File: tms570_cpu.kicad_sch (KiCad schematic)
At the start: 54 parts, among them J12 TSW-103-08-F-S-RA, J3 FTSH-105-01-L-DV-K, U2 TMS570LS0914APGEQQ1

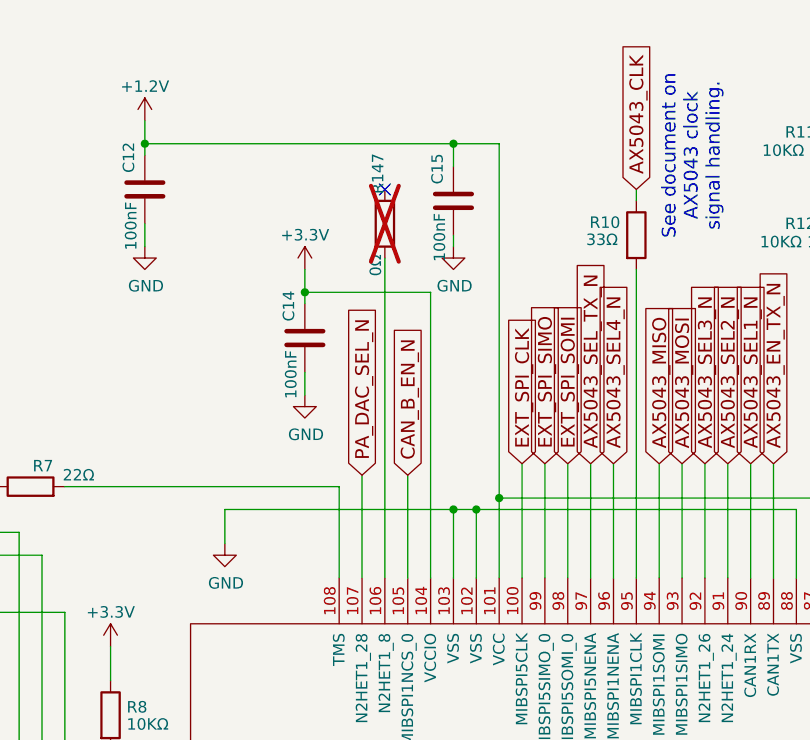
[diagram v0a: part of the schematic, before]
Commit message: Add switches on SPI to PC104, rework ICD and Design docs
Signed-off-by: Corey Minyard <corey@minyard.net>
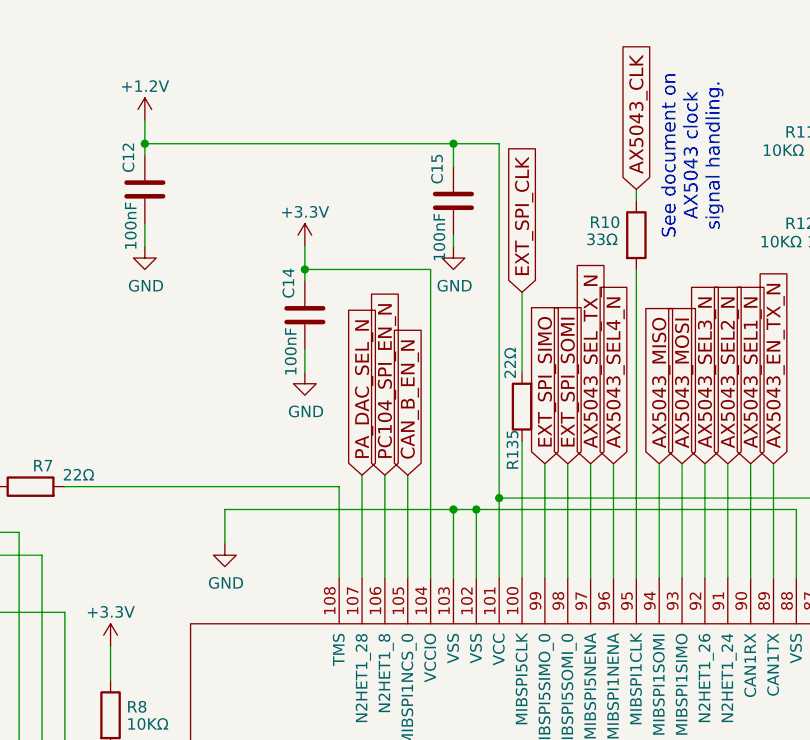
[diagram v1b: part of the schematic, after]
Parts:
- removed R147: 0Ω, Resistor_SMD:R_0402_1005Metric_Pad0.72x0.64mm_HandSolder, symbol Device:R
- added R135: 22Ω, Resistor_SMD:R_0402_1005Metric_Pad0.72x0.64mm_HandSolder, symbol Device:R
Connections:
- net EXT_SPI_CLK: now also R135.2; no longer U2.100 (MIBSPI5CLK)
- net PC104_SPI_EN_N: now reaches U2.106 (N2HET1_8)
- new net: R135.1, U2.100 (MIBSPI5CLK)
- no-connect marks 6 -> 5
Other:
- moved on the sheet: C14
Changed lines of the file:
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@@
 	)
 	(junction
-		(at 167.64 40.64)
+		(at 167.64 38.1)
 		(diameter 0)
 		(color 0 0 0 0)
@@
 	)
 	(no_connect
-		(at 176.53 29.21)
-	)
-	(no_connect
 		(at 247.65 52.07)
 	)
@@
 	(wire
 		(pts
-			(xy 167.64 49.53) (xy 167.64 52.07)
+			(xy 167.64 46.99) (xy 167.64 49.53)
 		)
 		(stroke
@@
 	(wire
 		(pts
-			(xy 167.64 38.1) (xy 167.64 40.64)
+			(xy 167.64 35.56) (xy 167.64 38.1)
 		)
 		(stroke
@@
 	(wire
 		(pts
+			(xy 176.53 60.96) (xy 176.53 72.39)
+		)
+		(stroke
+			(width 0)
+			(type default)
+		)
+	)
+	(wire
+		(pts
 			(xy 207.01 204.47) (xy 207.01 226.06)
 		)
@@
 	(wire
 		(pts
-			(xy 167.64 40.64) (xy 167.64 41.91)
+			(xy 167.64 38.1) (xy 167.64 39.37)
 		)
 		(stroke
@@
 	(wire
 		(pts
-			(xy 176.53 36.83) (xy 176.53 72.39)
-		)
-		(stroke
-			(width 0)
-			(type default)
-		)
-	)
-	(wire
-		(pts
 			(xy 110.49 187.96) (xy 116.84 187.96)
 		)
@@
 	(wire
 		(pts
-			(xy 181.61 40.64) (xy 181.61 72.39)
+			(xy 181.61 38.1) (xy 181.61 72.39)
 		)
 		(stroke
@@
 	(wire
 		(pts
-			(xy 167.64 40.64) (xy 181.61 40.64)
+			(xy 167.64 38.1) (xy 181.61 38.1)
 		)
 		(stroke
@@
 	(wire
 		(pts
+			(xy 191.77 57.15) (xy 191.77 72.39)
+		)
+		(stroke
+			(width 0)
+			(type default)
+		)
+	)
+	(wire
+		(pts
 			(xy 281.94 137.16) (xy 293.37 137.16)
 		)
@@
 	(wire
 		(pts
-			(xy 191.77 59.69) (xy 191.77 72.39)
+			(xy 191.77 40.64) (xy 191.77 49.53)
 		)
 		(stroke
@@
 		)
 	)
+	(global_label "PC104_SPI_EN_N"
+		(shape input)
+		(at 176.53 60.96 90)
+		(fields_autoplaced yes)
+		(effects
+			(font
+				(size 1.524 1.524)
+			)
+			(justify left)
+		)
+		(property "Intersheetrefs" "${INTERSHEET_REFS}"
+			(at 176.53 39.0045 90)
+			(effects
+				(font
+					(size 1.27 1.27)
+				)
+				(justify left)
+				(hide yes)
+			)
+		)
+	)
 	(global_label "AX5043_EN_RX3_N"
 		(shape input)
@@
 	(global_label "EXT_SPI_CLK"
 		(shape input)
-		(at 191.77 59.69 90)
+		(at 191.77 40.64 90)
 		(fields_autoplaced yes)
 		(effects
@@
 		)
 		(property "Intersheetrefs" "${INTERSHEET_REFS}"
-			(at 191.77 42.5968 90)
+			(at 191.77 23.5468 90)
 			(effects
 				(font
@@
 	(symbol
 		(lib_id "power:GND")
-		(at 167.64 52.07 0)
+		(at 167.64 49.53 0)
 		(unit 1)
 		(exclude_from_sim no)
@@
 		(dnp no)
 		(property "Reference" "#PWR023"
-			(at 167.64 58.42 0)
+			(at 167.64 55.88 0)
 			(effects
 				(font
@@
 		)
 		(property "Value" "GND"
-			(at 167.767 56.4642 0)
+			(at 167.767 53.9242 0)
 			(effects
 				(font
@@
 		)
 		(property "Footprint" ""
-			(at 167.64 52.07 0)
+			(at 167.64 49.53 0)
 			(effects
 				(font
@@
 		)
 		(property "Datasheet" ""
-			(at 167.64 52.07 0)
+			(at 167.64 49.53 0)
 			(effects
 				(font
@@
 		)
 		(property "Description" ""
-			(at 167.64 52.07 0)
+			(at 167.64 49.53 0)
 			(effects
 				(font
@@
 	(symbol
 		(lib_id "Device:R")
-		(at 176.53 33.02 0)
-		(unit 1)
-		(exclude_from_sim no)
-		(in_bom no)
-		(on_board yes)
-		(dnp yes)
-		(property "Reference" "R147"
-			(at 175.768 29.718 90)
-			(effects
-				(font
-					(size 1.27 1.27)
-				)
-				(justify left)
-			)
-		)
-		(property "Value" "0Ω"
-			(at 175.514 38.862 90)
-			(effects
-				(font
-					(size 1.27 1.27)
-				)
-				(justify left)
-			)
-		)
-		(property "Footprint" "Resistor_SMD:R_0402_1005Metric_Pad0.72x0.64mm_HandSolder"
-			(at 174.752 33.02 90)
-			(effects
-				(font
-					(size 1.27 1.27)
-				)
-				(hide yes)
-			)
-		)
-		(property "Datasheet" "~"
-			(at 176.53 33.02 0)
-			(effects
-				(font
-					(size 1.27 1.27)
-				)
-				(hide yes)
-			)
-		)
-		(property "Description" ""
-			(at 176.53 33.02 0)
-			(effects
-				(font
-					(size 1.27 1.27)
-				)
-			)
-		)
-		(pin "1"
-		)
-		(pin "2"
-		)
-		(instances
-			(project "PacSat_AFSK"
-				(path "/cc9f42d2-6985-41ac-acab-5ab7b01c5b38/adf61ae3-df77-4e04-8bda-b4049a36fcf4"
-					(reference "R147")
-					(unit 1)
-				)
-			)
-		)
-	)
-	(symbol
-		(lib_id "Device:R")
 		(at 125.73 64.77 90)
 		(unit 1)
@@
 	(symbol
 		(lib_id "Device:C")
-		(at 167.64 45.72 0)
+		(at 167.64 43.18 0)
 		(unit 1)
 		(exclude_from_sim no)
@@
 		(dnp no)
 		(property "Reference" "C14"
-			(at 165.862 42.164 90)
+			(at 165.862 39.624 90)
 			(effects
 				(font
@@
 		)
 		(property "Value" "100nF"
-			(at 166.116 49.784 90)
+			(at 166.116 47.244 90)
 			(effects
 				(font
@@
 		)
 		(property "Footprint" "Capacitor_SMD:C_0402_1005Metric_Pad0.74x0.62mm_HandSolder"
-			(at 168.6052 49.53 0)
+			(at 168.6052 46.99 0)
 			(effects
 				(font
@@
 		)
 		(property "Datasheet" "~"
-			(at 167.64 45.72 0)
+			(at 167.64 43.18 0)
 			(effects
 				(font
@@
 		)
 		(property "Description" ""
-			(at 167.64 45.72 0)
+			(at 167.64 43.18 0)
 			(effects
 				(font
@@
 	(symbol
 		(lib_id "power:+3.3V")
-		(at 167.64 38.1 0)
+		(at 167.64 35.56 0)
 		(unit 1)
 		(exclude_from_sim no)
@@
 		(fields_autoplaced yes)
 		(property "Reference" "#PWR022"
-			(at 167.64 41.91 0)
+			(at 167.64 39.37 0)
 			(effects
 				(font
@@
 		)
 		(property "Value" "+3.3V"
-			(at 167.64 34.29 0)
+			(at 167.64 31.75 0)
 			(effects
 				(font
@@
 		)
 		(property "Footprint" ""
-			(at 167.64 38.1 0)
+			(at 167.64 35.56 0)
 			(effects
 				(font
@@
 		)
 		(property "Datasheet" ""
-			(at 167.64 38.1 0)
+			(at 167.64 35.56 0)
 			(effects
 				(font
@@
 		)
 		(property "Description" ""
-			(at 167.64 38.1 0)
+			(at 167.64 35.56 0)
 			(effects
 				(font
@@
 					(unit 1)
 				)
+			)
+		)
+	)
+	(symbol
+		(lib_id "Device:R")
+		(at 191.77 53.34 180)
+		(unit 1)
+		(exclude_from_sim no)
+		(in_bom yes)
+		(on_board yes)
+		(dnp no)
+		(property "Reference" "R135"
+			(at 190.754 55.88 90)
+			(effects
+				(font
+					(size 1.27 1.27)
+				)
+				(justify left)
+			)
+		)
+		(property "Value" "22Ω"
+			(at 190.5 46.736 90)
+			(effects
+				(font
+					(size 1.27 1.27)
+				)
+				(justify left)
+			)
+		)
+		(property "Footprint" "Resistor_SMD:R_0402_1005Metric_Pad0.72x0.64mm_HandSolder"
+			(at 193.548 53.34 90)
+			(effects
+				(font
+					(size 1.27 1.27)
+				)
+				(hide yes)
+			)
+		)
+		(property "Datasheet" "~"
+			(at 191.77 53.34 0)
+			(effects
+				(font
+					(size 1.27 1.27)
+				)
+			)
+		)
+		(property "Description" ""
+			(at 191.77 53.34 0)
+			(effects
+				(font
+					(size 1.27 1.27)
+				)
+			)
+		)
+		(pin "1"
+		)
+		(pin "2"
+		)
+		(instances
+			(project "PacSat_AFSK"
+				(path "/cc9f42d2-6985-41ac-acab-5ab7b01c5b38/adf61ae3-df77-4e04-8bda-b4049a36fcf4"
+					(reference "R135")
+					(unit 1)
+				)

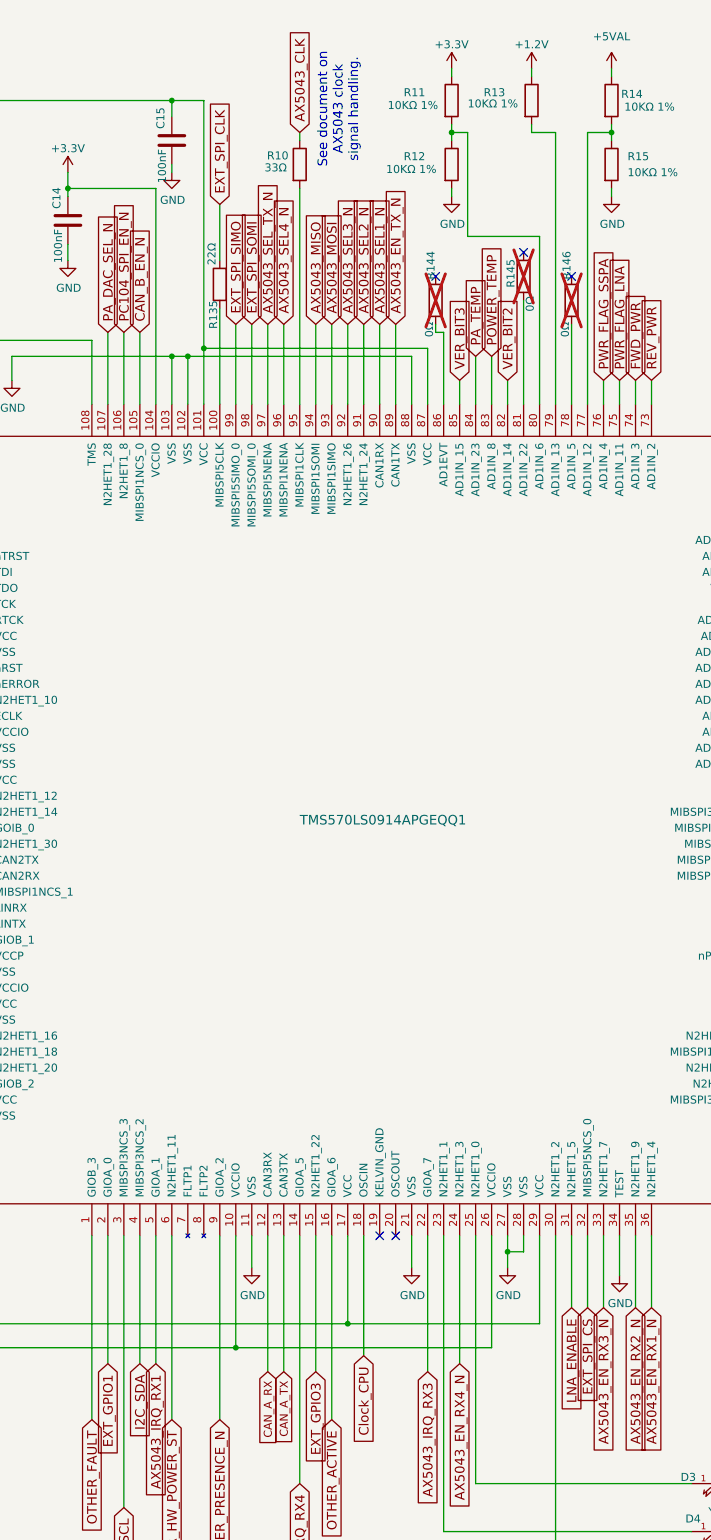
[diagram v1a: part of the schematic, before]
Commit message: Add a connection for an external antenna controller
Remove the SPI connection to the PC104 and use it for a SPI to I2C
converter microprocessor.  Add a connector for the external antenna
controller.

Signed-off-by: Corey Minyard <corey@minyard.net>
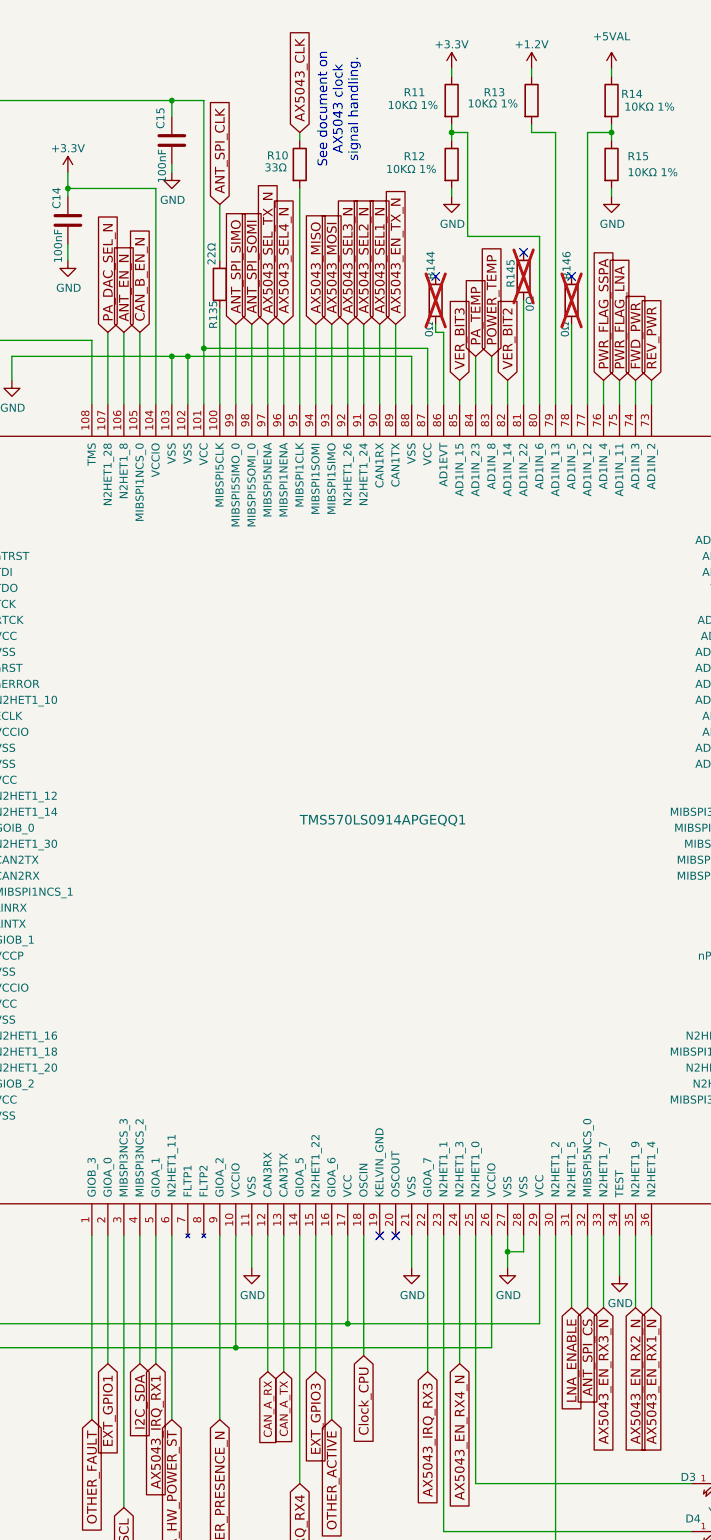
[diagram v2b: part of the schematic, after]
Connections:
- net EXT_SPI_CLK renamed ANT_SPI_CLK
- net EXT_SPI_CS renamed ANT_SPI_CS
- net EXT_SPI_SIMO renamed ANT_SPI_SIMO
- net EXT_SPI_SOMI renamed ANT_SPI_SOMI
- net PC104_SPI_EN_N renamed ANT_EN_N
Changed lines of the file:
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@@
 		)
 	)
-	(global_label "EXT_SPI_SIMO"
+	(global_label "ANT_SPI_SIMO"
 		(shape input)
 		(at 194.31 59.69 90)
@@
 		)
 		(property "Intersheetrefs" "${INTERSHEET_REFS}"
-			(at 194.31 41.3631 90)
+			(at 194.31 41.2905 90)
 			(effects
 				(font
@@
 		)
 	)
-	(global_label "PC104_SPI_EN_N"
+	(global_label "ANT_EN_N"
 		(shape input)
 		(at 176.53 60.96 90)
@@
 		)
 		(property "Intersheetrefs" "${INTERSHEET_REFS}"
-			(at 176.53 39.0045 90)
+			(at 176.53 47.2049 90)
 			(effects
 				(font
@@
 		)
 	)
-	(global_label "EXT_SPI_CLK"
+	(global_label "ANT_SPI_CLK"
 		(shape input)
 		(at 191.77 40.64 90)
@@
 		)
 		(property "Intersheetrefs" "${INTERSHEET_REFS}"
-			(at 191.77 23.5468 90)
+			(at 191.77 23.4742 90)
 			(effects
 				(font
@@
 		)
 	)
-	(global_label "EXT_SPI_CS"
+	(global_label "ANT_SPI_CS"
 		(shape input)
 		(at 250.19 215.9 270)
@@
 		)
 		(property "Intersheetrefs" "${INTERSHEET_REFS}"
-			(at 250.19 231.6869 90)
+			(at 250.19 231.7595 90)
 			(effects
 				(font
@@
 		)
 	)
-	(global_label "EXT_SPI_SOMI"
+	(global_label "ANT_SPI_SOMI"
 		(shape input)
 		(at 196.85 59.69 90)
@@
 		)
 		(property "Intersheetrefs" "${INTERSHEET_REFS}"
-			(at 196.85 41.3631 90)
-			(effects
-				(font
+			(at 196.85 41.2905 90)
+			(effects
+				(font
